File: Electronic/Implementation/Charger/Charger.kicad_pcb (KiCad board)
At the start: 2 copper layers, 46 x 28 mm, 16 parts, among them J1 Jack-DC, J2 66200221022, Q1 Q_PMOS_GSD, U1 MCP73844T-820I

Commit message: Charger - save with KiCad 6.0
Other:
- net class Default removed

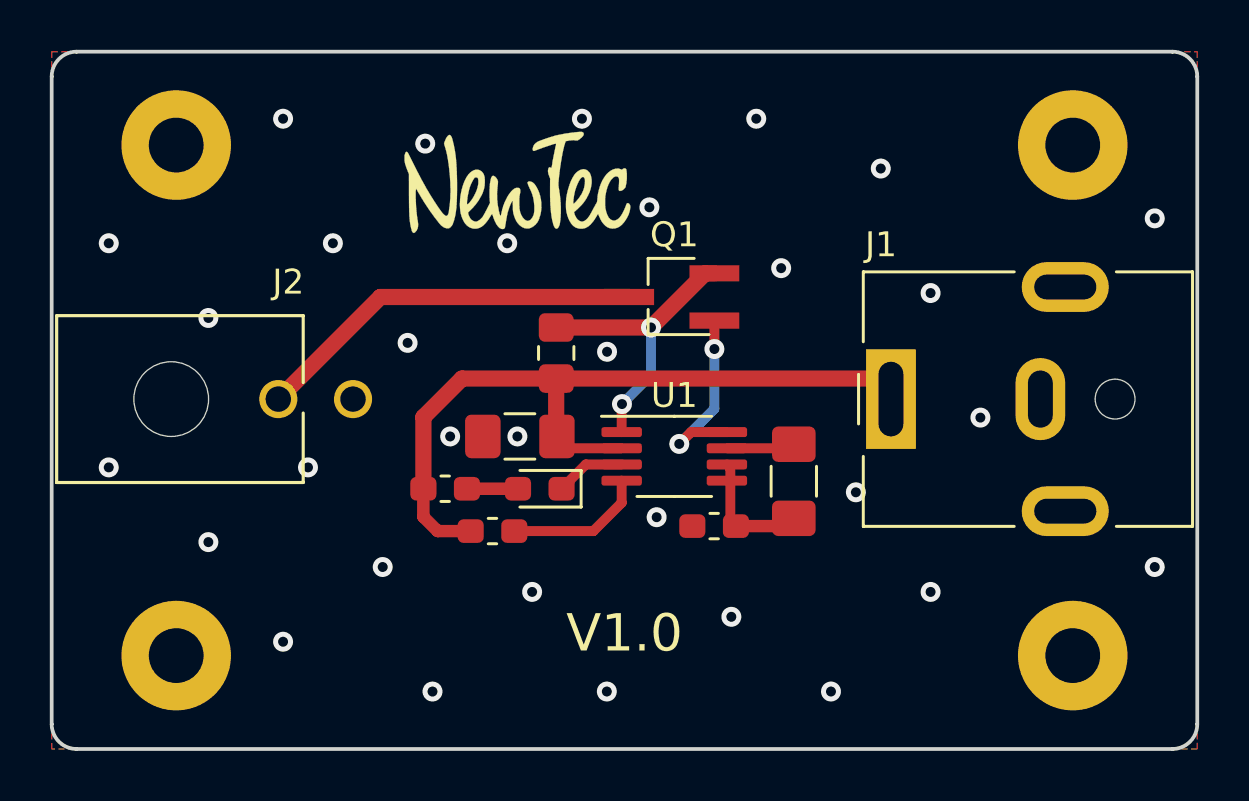
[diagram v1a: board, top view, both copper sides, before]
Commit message: Charger - place Text (Name, Repository) - set Vias
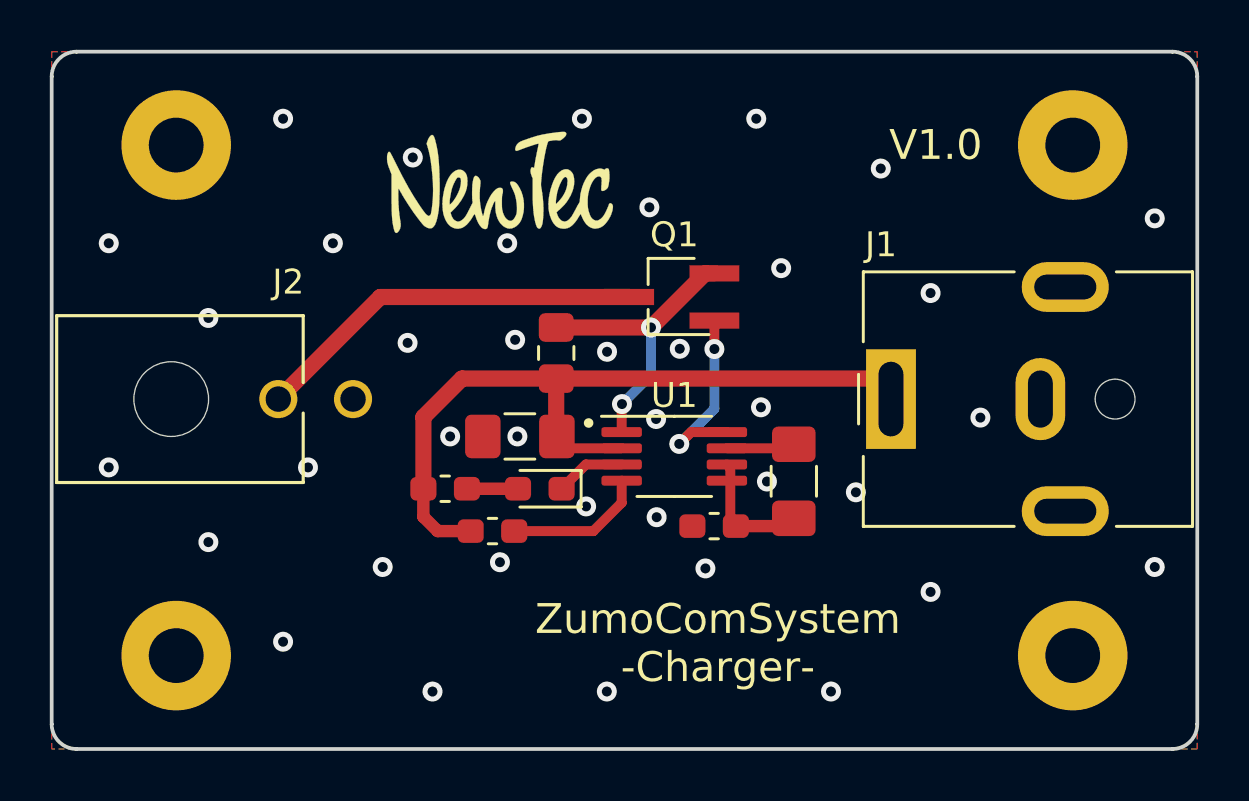
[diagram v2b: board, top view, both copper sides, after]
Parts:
- moved G*** 0.70 mm to (146.0, 79.5)
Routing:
- net GNDREF: vias 32 -> 38
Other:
- board text added: "${REVISION}"
- board text added: "Github Repository:"
- board text added: "NewTec-GmbH/ZumoComSystem"
- board text added: "ZumoComSystem -Charger-"
- board text removed: "V1.0"
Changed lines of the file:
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@@
   (paper "A4")
   (title_block
-    (date "2022-05-27")
+    (date "2022-08-12")
     (rev "V1.0")
   )
@@
   )
   (footprint "footprints:NT_Kicad_Logo_2500x2500" (layer "F.Cu")
-    (at 146.7 79.5)
+    (at 146 79.5)
     (attr through_hole)
     (fp_text reference "G***" (at 0 0) (layer "F.SilkS") hide
@@
     )
   )
+  (gr_line (start 143.125 97) (end 160.375 97) (layer "B.SilkS") (width 0.2))
+  (gr_circle (center 149.56 89.16) (end 149.652195 89.16) (layer "F.SilkS") (width 0.2) (fill none))
   (gr_line (start 173 74.25) (end 129 74.25) (layer "Edge.Cuts") (width 0.15))
   (gr_arc (start 174 101.25) (mid 173.707107 101.957107) (end 173 102.25) (layer "Edge.Cuts") (width 0.15))
@@
   (gr_line (start 174 101.25) (end 174 75.25) (layer "Edge.Cuts") (width 0.15))
   (gr_line (start 128 75.25) (end 128 101.25) (layer "Edge.Cuts") (width 0.15))
-  (gr_text "V1.0" (at 151 97.6) (layer "F.SilkS")
-    (effects (font (size 1.5 1.5) (thickness 0.3)))
+  (gr_text "Github Repository:" (at 151.75 95.75) (layer "B.SilkS")
+    (effects (font (size 1.2 1.2) (thickness 0.2)) (justify mirror))
+  )
+  (gr_text "NewTec-GmbH/ZumoComSystem" (at 151.5 98.25) (layer "B.SilkS")
+    (effects (font (size 1 1) (thickness 0.15) italic) (justify mirror))
+  )
+  (gr_text "ZumoComSystem\n-Charger- \n" (at 154.75 98) (layer "F.SilkS")
+    (effects (font (size 1.2 1.2) (thickness 0.25)))
+  )
+  (gr_text "${REVISION}" (at 163.5 78) (layer "F.SilkS")
+    (effects (font (size 1.2 1.2) (thickness 0.2)))
   )
   (gr_text "BOT" (at 139 100) (layer "B.Mask")
@@
   (via (at 150.291667 99.9425) (size 0.8) (drill 0.4) (layers "F.Cu" "B.Cu") (net 1))
   (via (at 141.291667 94.9425) (size 0.8) (drill 0.4) (layers "F.Cu" "B.Cu") (net 1))
+  (via (at 156.48 88.53) (size 0.8) (drill 0.4) (layers "F.Cu" "B.Cu") (free) (net 1))
   (via (at 138.291667 90.9425) (size 0.8) (drill 0.4) (layers "F.Cu" "B.Cu") (net 1))
   (via (at 161.291667 78.9425) (size 0.8) (drill 0.4) (layers "F.Cu" "B.Cu") (net 1))
+  (via (at 156.72 91.51) (size 0.8) (drill 0.4) (layers "F.Cu" "B.Cu") (free) (net 1))
   (via (at 172.291667 94.9425) (size 0.8) (drill 0.4) (layers "F.Cu" "B.Cu") (net 1))
+  (via (at 152.27 89) (size 0.8) (drill 0.4) (layers "F.Cu" "B.Cu") (free) (net 1))
   (via (at 163.291667 83.9425) (size 0.8) (drill 0.4) (layers "F.Cu" "B.Cu") (net 1))
   (via (at 165.291667 88.9425) (size 0.8) (drill 0.4) (layers "F.Cu" "B.Cu") (net 1))
   (via (at 134.291667 93.9425) (size 0.8) (drill 0.4) (layers "F.Cu" "B.Cu") (net 1))
+  (via (at 146.61 85.82) (size 0.8) (drill 0.4) (layers "F.Cu" "B.Cu") (free) (net 1))
   (via (at 144 89.7) (size 0.8) (drill 0.4) (layers "F.Cu" "B.Cu") (net 1))
   (via (at 130.291667 81.9425) (size 0.8) (drill 0.4) (layers "F.Cu" "B.Cu") (net 1))
@@
   (via (at 159.291667 99.9425) (size 0.8) (drill 0.4) (layers "F.Cu" "B.Cu") (net 1))
   (via (at 143.291667 99.9425) (size 0.8) (drill 0.4) (layers "F.Cu" "B.Cu") (net 1))
+  (via (at 153.22 86.18) (size 0.8) (drill 0.4) (layers "F.Cu" "B.Cu") (free) (net 1))
+  (via (at 149.46 92.51) (size 0.8) (drill 0.4) (layers "F.Cu" "B.Cu") (free) (net 1))
   (via (at 142.291667 85.9425) (size 0.8) (drill 0.4) (layers "F.Cu" "B.Cu") (net 1))
   (via (at 146.7 89.7) (size 0.8) (drill 0.4) (layers "F.Cu" "B.Cu") (net 1))
   (via (at 157.291667 82.9425) (size 0.8) (drill 0.4) (layers "F.Cu" "B.Cu") (net 1))
-  (via (at 143 77.9425) (size 0.8) (drill 0.4) (layers "F.Cu" "B.Cu") (net 1))
+  (via (at 142.5 78.5) (size 0.8) (drill 0.4) (layers "F.Cu" "B.Cu") (net 1))
   (via (at 160.291667 91.9425) (size 0.8) (drill 0.4) (layers "F.Cu" "B.Cu") (net 1))
   (via (at 137.291667 97.9425) (size 0.8) (drill 0.4) (layers "F.Cu" "B.Cu") (net 1))
   (via (at 139.291667 81.9425) (size 0.8) (drill 0.4) (layers "F.Cu" "B.Cu") (net 1))
-  (via (at 147.291667 95.9425) (size 0.8) (drill 0.4) (layers "F.Cu" "B.Cu") (net 1))
+  (via (at 146 94.75) (size 0.8) (drill 0.4) (layers "F.Cu" "B.Cu") (net 1))
   (via (at 134.291667 84.9425) (size 0.8) (drill 0.4) (layers "F.Cu" "B.Cu") (net 1))
   (via (at 137.291667 76.9425) (size 0.8) (drill 0.4) (layers "F.Cu" "B.Cu") (net 1))
   (via (at 163.291667 95.9425) (size 0.8) (drill 0.4) (layers "F.Cu" "B.Cu") (net 1))
-  (via (at 155.291667 96.9425) (size 0.8) (drill 0.4) (layers "F.Cu" "B.Cu") (net 1))
+  (via (at 154.25 95) (size 0.8) (drill 0.4) (layers "F.Cu" "B.Cu") (net 1))
   (segment (start 142.925 92.925) (end 143.5 93.5) (width 0.5) (layer "F.Cu") (net 2))
   (segment (start 160.875 87.375) (end 161.7 88.2) (width 0.65) (layer "F.Cu") (net 2))
@@
   (segment (start 146.575 93.5) (end 149.75 93.5) (width 0.4) (layer "F.Cu") (net 10))
   (zone (net 1) (net_name "GNDREF") (layer "F.Cu") (hatch edge 0.508)
-    (connect_pads (clearance 0.508))
-    (min_thickness 0.254)
-    (fill yes (thermal_gap 0.508) (thermal_bridge_width 0.508))
+    (connect_pads (clearance 0.4))
+    (min_thickness 0.2) (filled_areas_thickness no)
+    (fill yes (thermal_gap 0.4) (thermal_bridge_width 0.4))
     (polygon
       (pts
@@
   )
   (zone (net 1) (net_name "GNDREF") (layer "B.Cu") (hatch edge 0.508)
-    (connect_pads (clearance 0.508))
-    (min_thickness 0.254)
-    (fill yes (thermal_gap 0.508) (thermal_bridge_width 0.508))
+    (connect_pads (clearance 0.4))
+    (min_thickness 0.2) (filled_areas_thickness no)
+    (fill yes (thermal_gap 0.4) (thermal_bridge_width 0.4))
     (polygon
       (pts
